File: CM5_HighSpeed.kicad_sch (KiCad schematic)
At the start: 63 parts, among them J1 USB-C, J10 USB-C, J15 USB_C_Receptacle, J17 USB-C, J22 Conn_HDMI, J5 Conn_1x22_Female, J6 USB-C, U11 TUSB4041I, U12 RT9742SNGV, U13 TLV75712PDBVR, U15 AP22653W6, U6 AP22653W6, Y1 ECS-2520MV-240-CN-TR

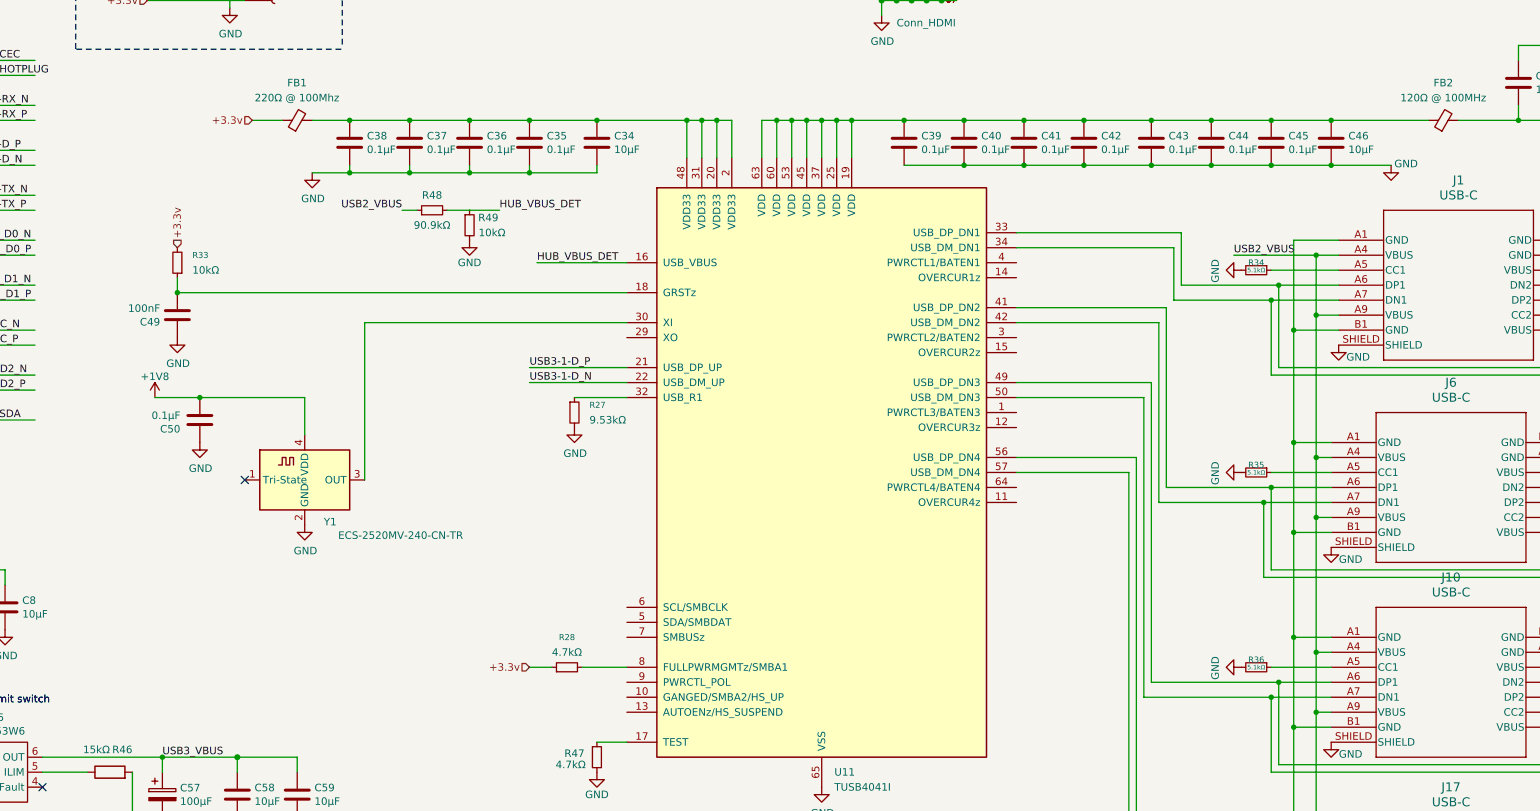
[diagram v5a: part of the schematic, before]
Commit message: USB hub: hold GRSTz with a TPS3808 supervisor on the core rail
GRSTz (U11 pin 18) only had a 10k/100nF RC from +3.3 V (~1 ms to VIH).
TI requires the reset held >= 3 ms after both VDD33 and VDD are stable,
and an active reset whenever VDD33 is up before VDD (TUSB4041I 5.6,
6.3.7) - which is always the case here, since the core LDO runs from
3.3 V.

- New U19 TPS3808G01DBVR (SOT-23-6), powered from +3.3v (C72 0.1 uF),
  senses the hub core rail (new label HUB_VDD, hub side of FB2) through
  R50 158k / R51 100k: trip = 0.405 V x 2.58 = 1.045 V (1.01-1.08 V
  worst case) on the 1.2 V rail; hub VDD minimum is 0.99 V. C73 1 nF on
  SENSE per the TPS3808 datasheet.
- CT left open: 20 ms typical (12 ms min) reset delay after the rail is
  good. MR left open (internal pull-up).
- Open-drain RESET drives GRSTz (label HUB_GRSTz) into the existing
  R33 10k pull-up to 3.3 V. RESET stays low while SENSE is below the
  threshold, so the hub is held in reset until 3.3 V, 1.8 V (clock)
  and 1.2 V are all up.
- C49 (100 nF on GRSTz) removed: discharging it through the open-drain
  output would exceed the TPS3808 RESET pin current rating.

Digikey numbers for U19, R50, R51, C72 and C73 were not confirmed
against live listings; check when ordering.

Refs #25 (verify on hardware before closing).

Co-Authored-By: Claude Opus 5.5 <noreply@anthropic.com>
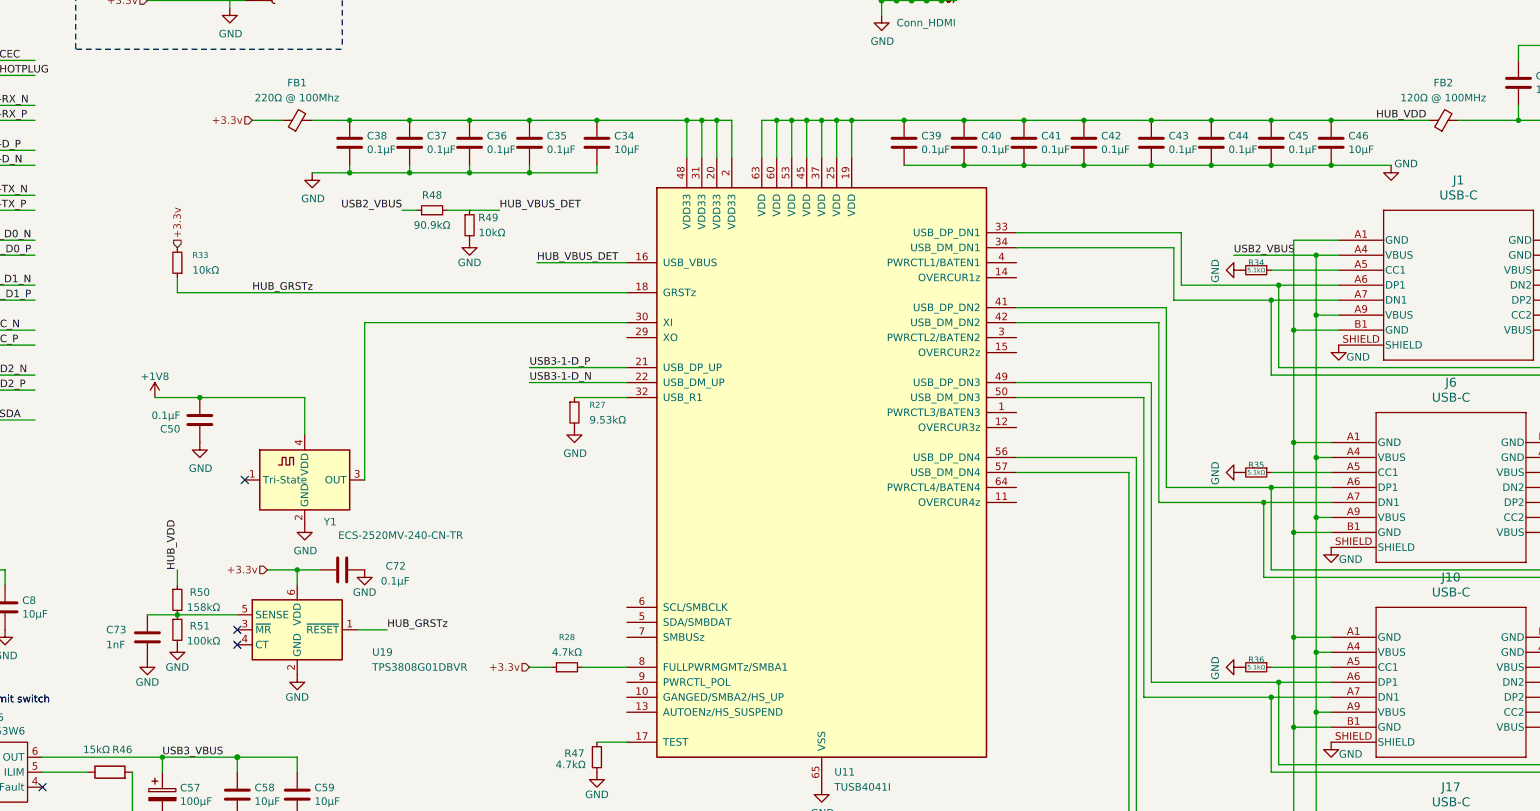
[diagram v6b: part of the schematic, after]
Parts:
- removed C49: 100nF, Capacitor_SMD:C_0402_1005Metric, symbol Device:C
- added C72: 0.1µF, Capacitor_SMD:C_0603_1608Metric, symbol Device:C
- added C73: 1nF, Capacitor_SMD:C_0603_1608Metric, symbol Device:C
- added R50: 158kΩ, Resistor_SMD:R_0603_1608Metric, symbol Device:R_Small
- added R51: 100kΩ, Resistor_SMD:R_0603_1608Metric, symbol Device:R_Small
- added U19: TPS3808G01DBVR, Package_TO_SOT_SMD:SOT-23-6, symbol Power_Supervisor:TPS3808DBV
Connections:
- net +3.3v: now also C72.1, U19.6 (VDD)
- net GND: now also C72.2, C73.2, R51.2, U19.2 (GND)
- net HUB_VDD: now reaches C39.1, C40.1, C41.1, C42.1, C43.1, C44.1, C45.1, C46.1, FB2.1, U11.19 (VDD), U11.25 (VDD), U11.37 (VDD), U11.45 (VDD), U11.53 (VDD), U11.60 (VDD), U11.63 (VDD)
- net HUB_VDD: now also R50.1
- net HUB_GRSTz: now reaches R33.1, U11.18 (GRSTz)
- net HUB_GRSTz: now also U19.1 (~{RESET})
- new net: C73.1, R50.2, R51.1, U19.5 (SENSE)
- no-connect marks 4 -> 6

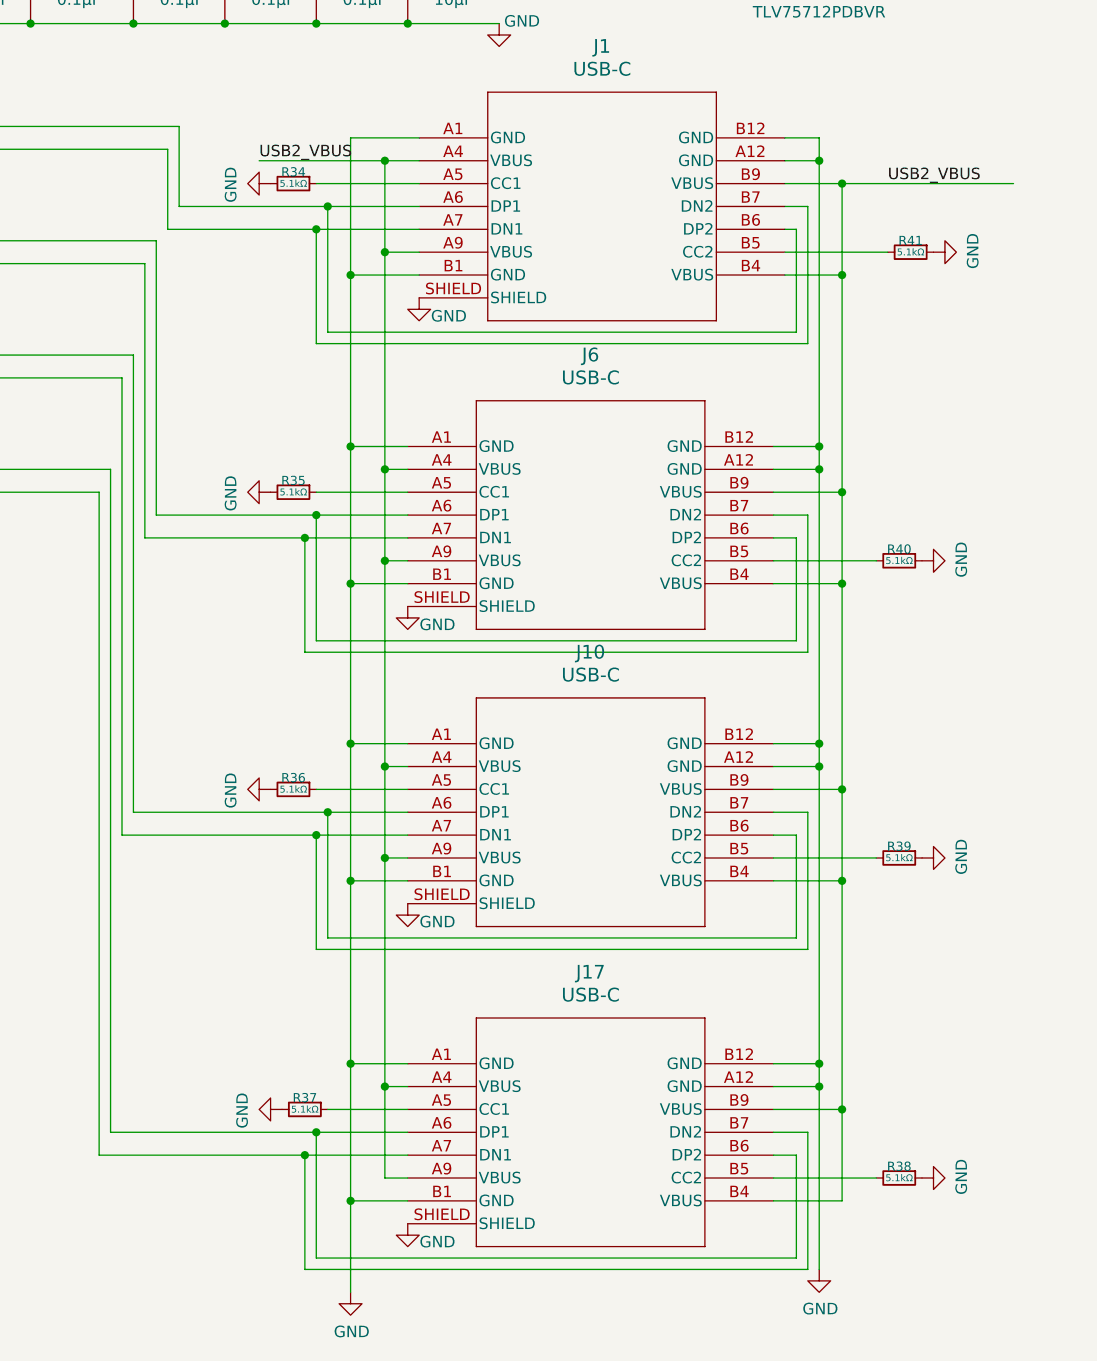
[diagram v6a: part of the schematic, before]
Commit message: USB hub ports: CC pins get 56k Rp pull-ups to VBUS instead of 5.1k Rd
R34-R41 pulled CC1/CC2 of the four hub USB-C ports (J1, J6, J10, J17)
to GND through 5.1k. That is Rd, the signature of a USB-C *sink*, on
ports that are meant to be hosts/sources. USB-A-to-C cables hide this,
but a proper C-to-C device may not attach, and a charger or another host
plugged in sees a sink and can push its own 5 V into USB2_VBUS.

Now 56k from each CC pin to USB2_VBUS: Rp for "Default USB Power"
(USB Type-C spec R2.0, Table 4-24, Rp pulled to 4.75-5.5 V). Default
power is the honest advertisement, since one 1.735 A switch (U6)
feeds all four ports.

0603, Panasonic ERJ-3EKF5602V (Digikey number not confirmed live).

Refs #22.

Co-Authored-By: Claude Opus 5.5 <noreply@anthropic.com>
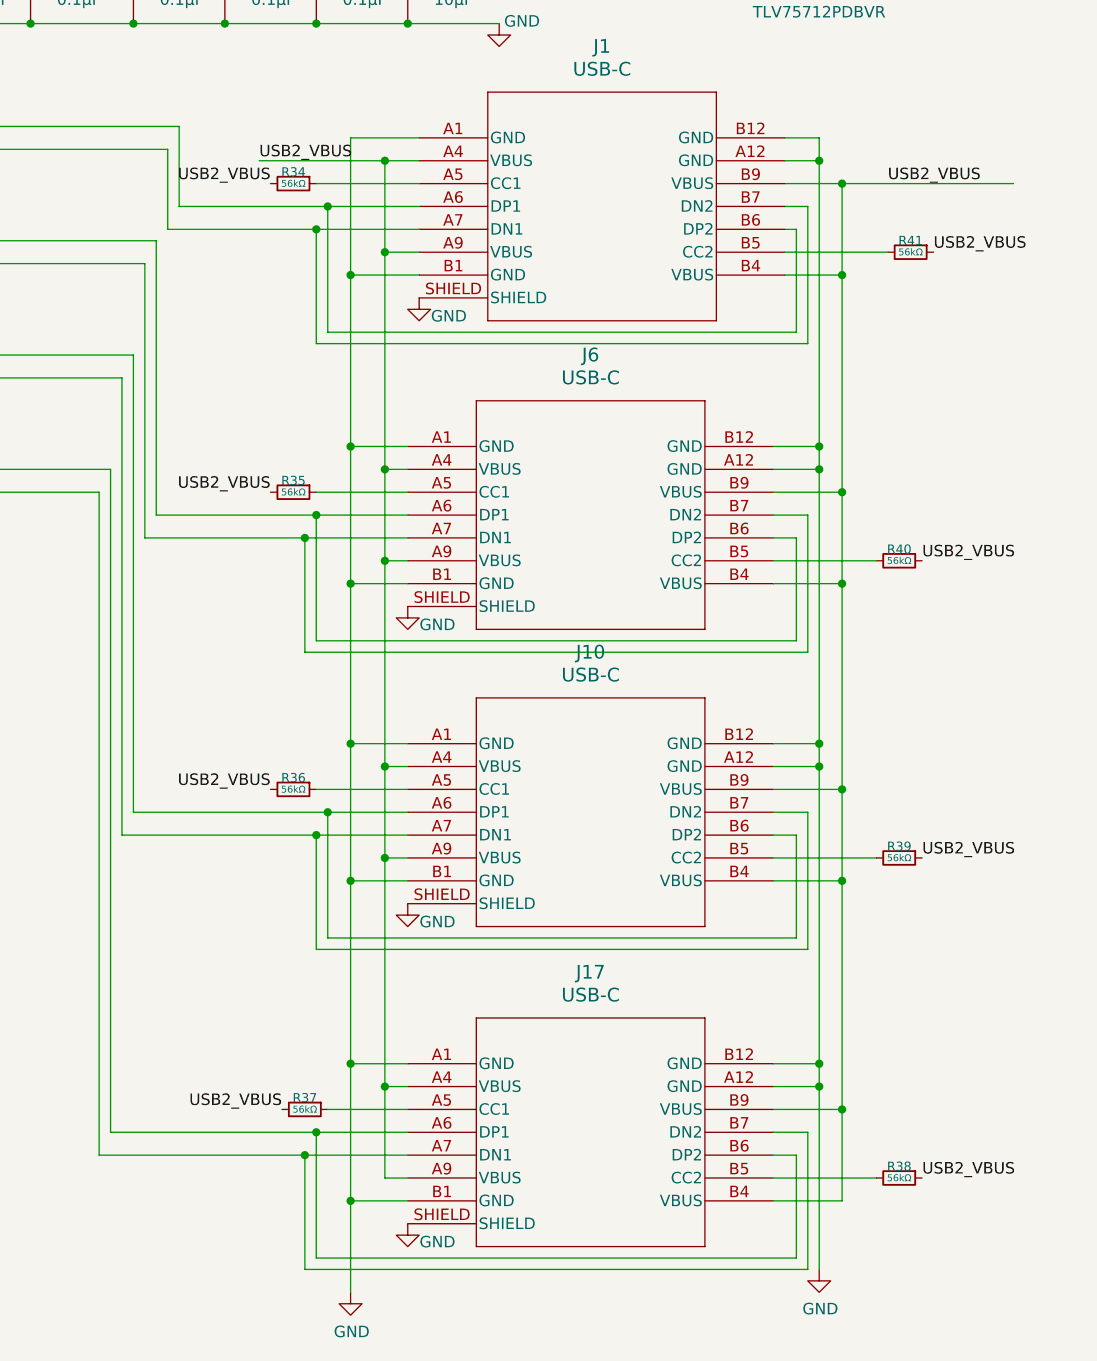
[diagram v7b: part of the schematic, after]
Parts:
- R34, R35, R36, R37, R38, R39, R40, R41: value 5.1kΩ -> 56kΩ; footprint Resistor_SMD:R_0402_1005Metric -> Resistor_SMD:R_0603_1608Metric; Dist. P/N P5.10KLTR-ND -> P56.0KHTR-ND; Manf. P/N ERJ-2RKF5101X -> ERJ-3EKF5602V; Part Description Resistor, 5.1kΩ, ±1%, 0.1W, SMD 0402 (1005m) -> Resistor, 56kΩ, ±1%, 0.1W, SMD 0603 (1608m)
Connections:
- net GND: no longer R34.2, R35.2, R36.2, R37.2, R38.1, R39.1, R40.1, R41.1
- net USB2_VBUS: now also R34.2, R35.2, R36.2, R37.2, R38.1, R39.1, R40.1, R41.1
